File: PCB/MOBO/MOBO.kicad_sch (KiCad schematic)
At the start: 10 parts, among them J101 COMP_OUT, J102 COMP_5V, J103 COMP_GND, J104 RPi_GPio, J105 JST_02, J106 RPi_SDA0, J107 RPi_TV, J108 RPi_D-, J109 RPi_D+, J110 RPi_SCL0

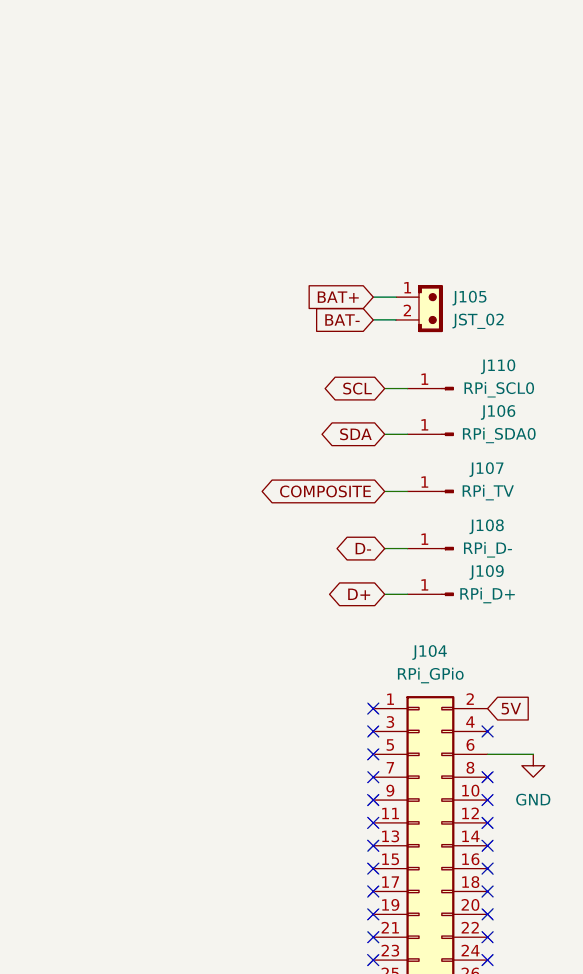
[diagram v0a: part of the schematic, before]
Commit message: fixed 5v RPi power rail to not bypass the internal RPi fuse
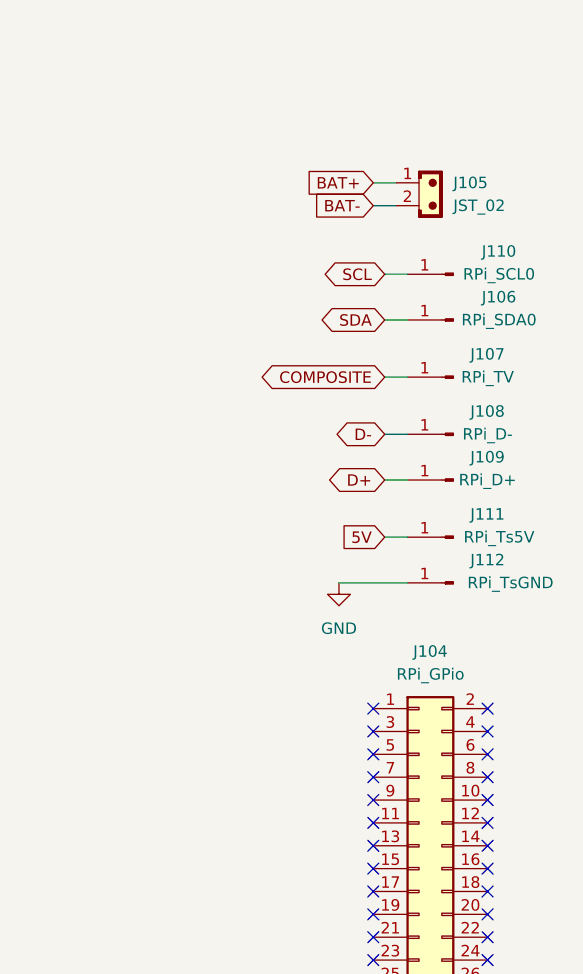
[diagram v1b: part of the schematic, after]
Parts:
- added J111: RPi_Ts5V, TestPoint:TestPoint_Pad_1.5x1.5mm, symbol Connector:Conn_01x01_Male
- added J112: RPi_TsGND, TestPoint:TestPoint_Pad_1.5x1.5mm, symbol Connector:Conn_01x01_Male
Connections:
- net 5V: now also J111.1 (Pin_1); no longer J104.2 (Pin_2)
- net GND: now also J112.1 (Pin_1); no longer J104.6 (Pin_6)
- no-connect marks 38 -> 40
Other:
- moved on the sheet: J105, J106, J107, J108, J109, J110

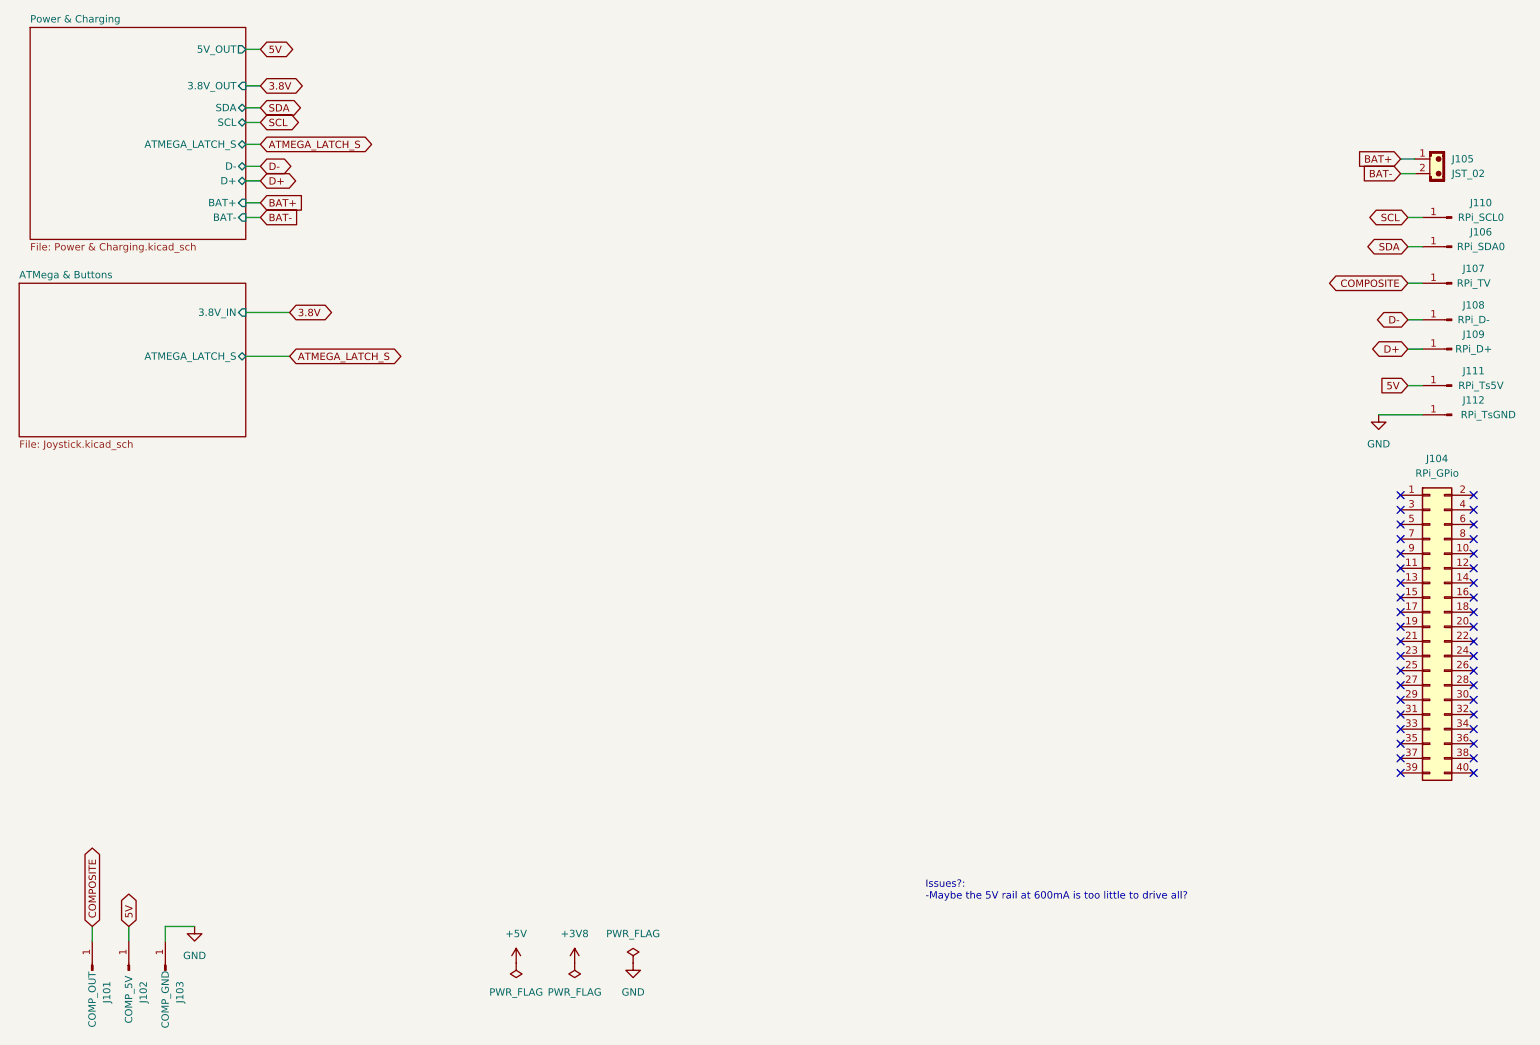
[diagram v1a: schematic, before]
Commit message: fixed testpoint footprint
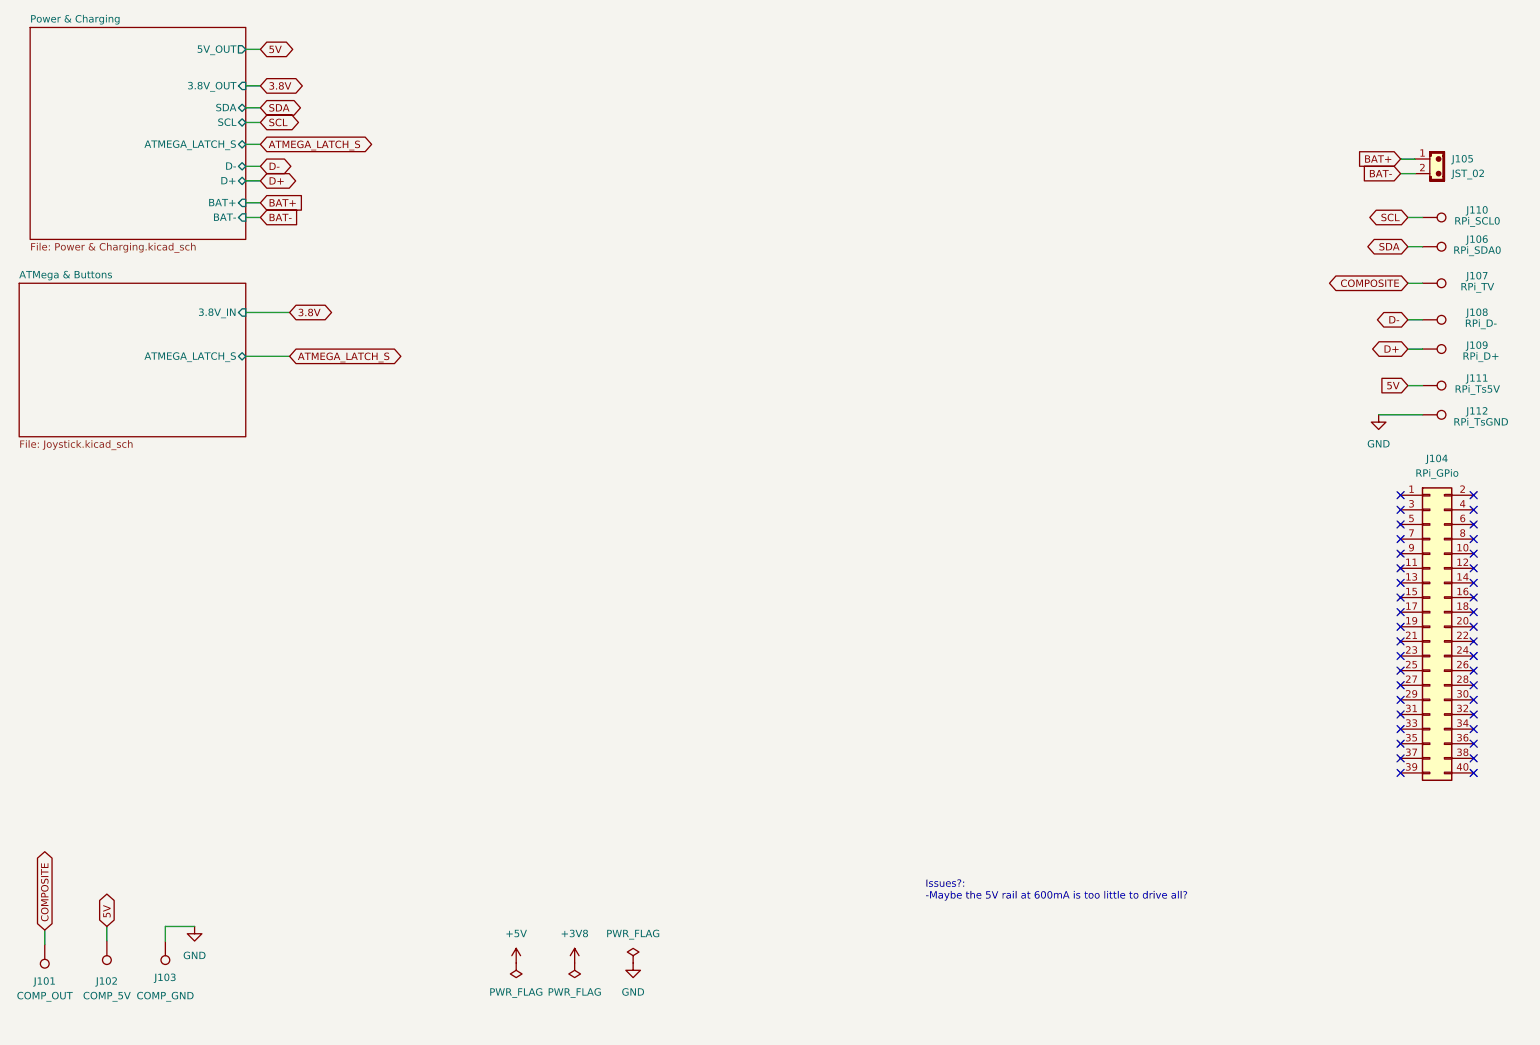
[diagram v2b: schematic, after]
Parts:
- J101, J102, J103, J106, J107, J108, J109, J110, J111, J112: symbol Connector:Conn_01x01_Male -> Connector:TestPoint

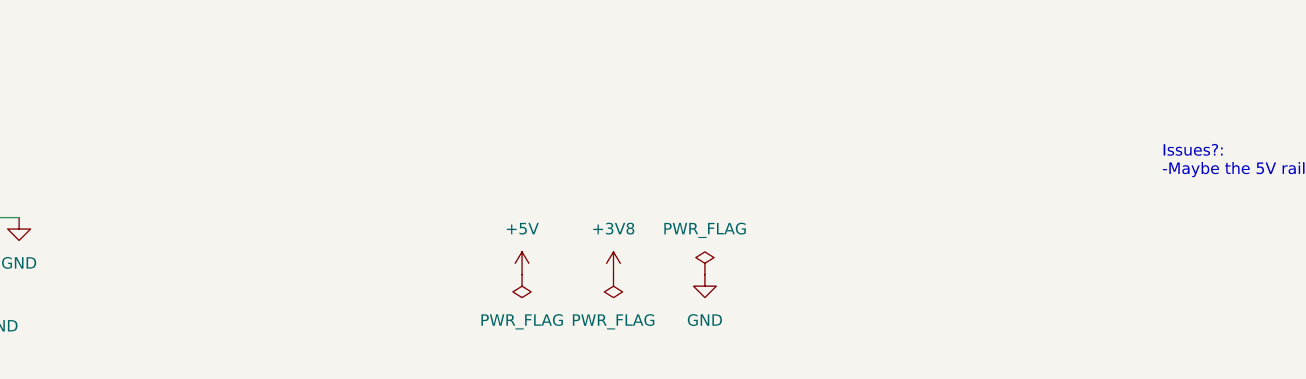
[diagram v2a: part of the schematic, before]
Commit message: added mounting holes
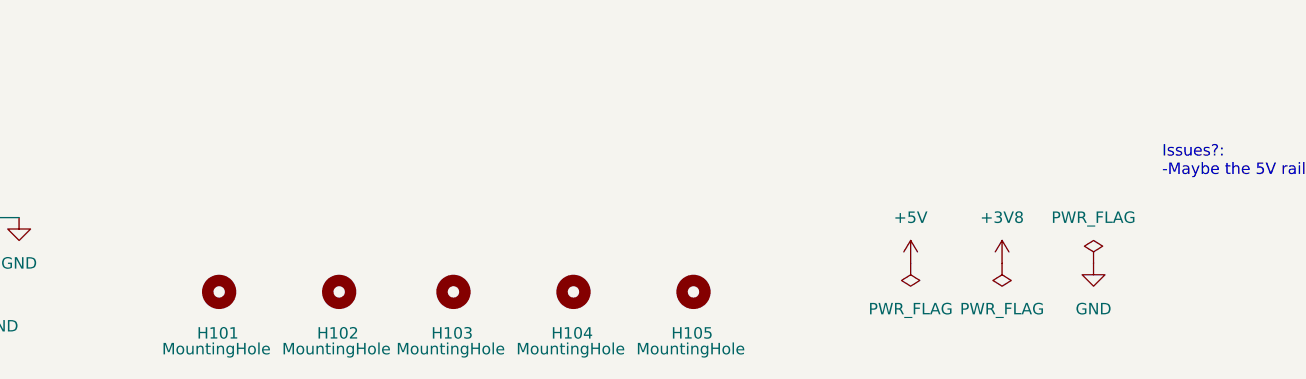
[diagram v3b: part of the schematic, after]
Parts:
- added H101, H102, H103, H104, H105: MountingHole, MountingHole:MountingHole_2.1mm, symbol Mechanical:MountingHole

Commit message: fixed rpi gpio footprint
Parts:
- J104: footprint Connector_PinHeader_2.00mm:PinHeader_2x20_P2.00mm_Vertical -> Connector_PinHeader_2.54mm:PinHeader_2x20_P2.54mm_Vertical
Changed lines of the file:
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@@
       (effects (font (size 1.27 1.27)))
     )
-    (property "Footprint" "Connector_PinHeader_2.00mm:PinHeader_2x20_P2.00mm_Vertical" (at 265.43 123.19 0)
+    (property "Footprint" "Connector_PinHeader_2.54mm:PinHeader_2x20_P2.54mm_Vertical" (at 265.43 123.19 0)
       (effects (font (size 1.27 1.27)) hide)
     )

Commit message: fixed schematic net names
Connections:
- net 5V is gone; now on net +5V: J102.1, J111.1
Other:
- sheet ATMega & Buttons ports: added none; removed 3.8V_IN
- sheet Power & Charging ports: added none; removed 3.8V_OUT, 5V_OUT
- moved on the sheet: H101, H102, H103, H104, H105

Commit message: Started pcb traces
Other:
- note added: "Battery connector"
- note added: "Composite screen output"
- note added: "RPi Pads"
- company: (none) -> ilnerdchuck
- title: Power Circuit -> GBA-SPi
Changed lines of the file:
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@@
   (paper "A4")
   (title_block
-    (title "Power Circuit")
+    (title "GBA-SPi")
     (date "2023-06-06")
-    (rev "0.1")
+    (rev "0.5")
+    (company "ilnerdchuck")
+    (comment 1 "Repo: https://github.com/ilnerdchuck/GBA-SPi")
   )
   (no_connect (at 273.05 138.43))
@@
     (stroke (width 0) (type default))
   )
-  (wire (pts (xy 256.54 86.36) (xy 264.16 86.36))
+  (wire (pts (xy 261.62 86.36) (xy 264.16 86.36))
     (stroke (width 0) (type default))
   )
@@
   (wire (pts (xy 59.69 33.02) (xy 62.23 33.02))
     (stroke (width 0) (type default))
+  )
+  (rectangle (start 244.475 48.26) (end 282.575 92.71)
+    (stroke (width 0) (type dash_dot_dot))
+    (fill (type none))
+  )
+  (rectangle (start 19.05 156.845) (end 53.34 188.595)
+    (stroke (width 0) (type dash_dot_dot))
+    (fill (type none))
+  )
+  (rectangle (start 244.475 38.1) (end 282.575 47.625)
+    (stroke (width 0) (type dash_dot_dot))
+    (fill (type none))
+  )
+  (text "Battery connector\n" (at 245.11 40.64 0)
+    (effects (font (size 1.27 1.27)) (justify left bottom))
+  )
+  (text "RPi Pads\n" (at 245.11 50.8 0)
+    (effects (font (size 1.27 1.27)) (justify left bottom))
+  )
+  (text "Composite screen\noutput\n" (at 22.225 161.29 0)
+    (effects (font (size 1.27 1.27)) (justify left bottom))
   )
   (text "Issues?:\n-Maybe the 5V rail at 600mA is too little to drive all?\n"
@@
     )
   )
-  (symbol (lib_id "power:GND") (at 256.54 86.36 0) (mirror y) (unit 1)
-    (in_bom yes) (on_board yes) (dnp no) (fields_autoplaced)
-    (property "Reference" "#PWR0102" (at 256.54 92.71 0)
-      (effects (font (size 1.27 1.27)) hide)
-    )
-    (property "Value" "GND" (at 256.54 91.44 0)
-      (effects (font (size 1.27 1.27)))
-    )
-    (property "Footprint" "" (at 256.54 86.36 0)
-      (effects (font (size 1.27 1.27)) hide)
-    )
-    (property "Datasheet" "" (at 256.54 86.36 0)
+  (symbol (lib_id "power:GND") (at 261.62 86.36 0) (mirror y) (unit 1)
+    (in_bom yes) (on_board yes) (dnp no) (fields_autoplaced)
+    (property "Reference" "#PWR0102" (at 261.62 92.71 0)
+      (effects (font (size 1.27 1.27)) hide)
+    )
+    (property "Value" "GND" (at 261.62 91.44 0)
+      (effects (font (size 1.27 1.27)))
+    )
+    (property "Footprint" "" (at 261.62 86.36 0)
+      (effects (font (size 1.27 1.27)) hide)
+    )
+    (property "Datasheet" "" (at 261.62 86.36 0)
       (effects (font (size 1.27 1.27)) hide)
     )
@@
   (symbol (lib_id "power:VBUS") (at 128.27 180.34 0) (unit 1)
     (in_bom yes) (on_board yes) (dnp no) (fields_autoplaced)
-    (property "Reference" "#PWR0218" (at 128.27 184.15 0)
+    (property "Reference" "#PWR0103" (at 128.27 184.15 0)
       (effects (font (size 1.27 1.27)) hide)
     )
@@
     (instances
       (project "MOBO"
-        (path "/2d62a3c1-c4f2-4921-9f6b-8dc8aef69d64/968b581c-59b8-4e39-ae9d-82f589704db7"
-          (reference "#PWR0218") (unit 1)
-        )
         (path "/2d62a3c1-c4f2-4921-9f6b-8dc8aef69d64"
           (reference "#PWR0103") (unit 1)
@@
   (symbol (lib_id "power:+5VA") (at 139.065 180.34 0) (unit 1)
     (in_bom yes) (on_board yes) (dnp no)
-    (property "Reference" "#PWR0226" (at 139.065 184.15 0)
+    (property "Reference" "#PWR0107" (at 139.065 184.15 0)
       (effects (font (size 1.27 1.27)) hide)
     )
@@
     (instances
       (project "MOBO"
-        (path "/2d62a3c1-c4f2-4921-9f6b-8dc8aef69d64/968b581c-59b8-4e39-ae9d-82f589704db7"
-          (reference "#PWR0226") (unit 1)
-        )
         (path "/2d62a3c1-c4f2-4921-9f6b-8dc8aef69d64"
           (reference "#PWR0107") (unit 1)

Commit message: fix: battery charging protection module
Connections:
- net BAT-: no longer J105.2
- net GND: now also J105.2
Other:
- moved on the sheet: J105
